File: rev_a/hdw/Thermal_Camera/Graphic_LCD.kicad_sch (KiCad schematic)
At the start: 0 parts

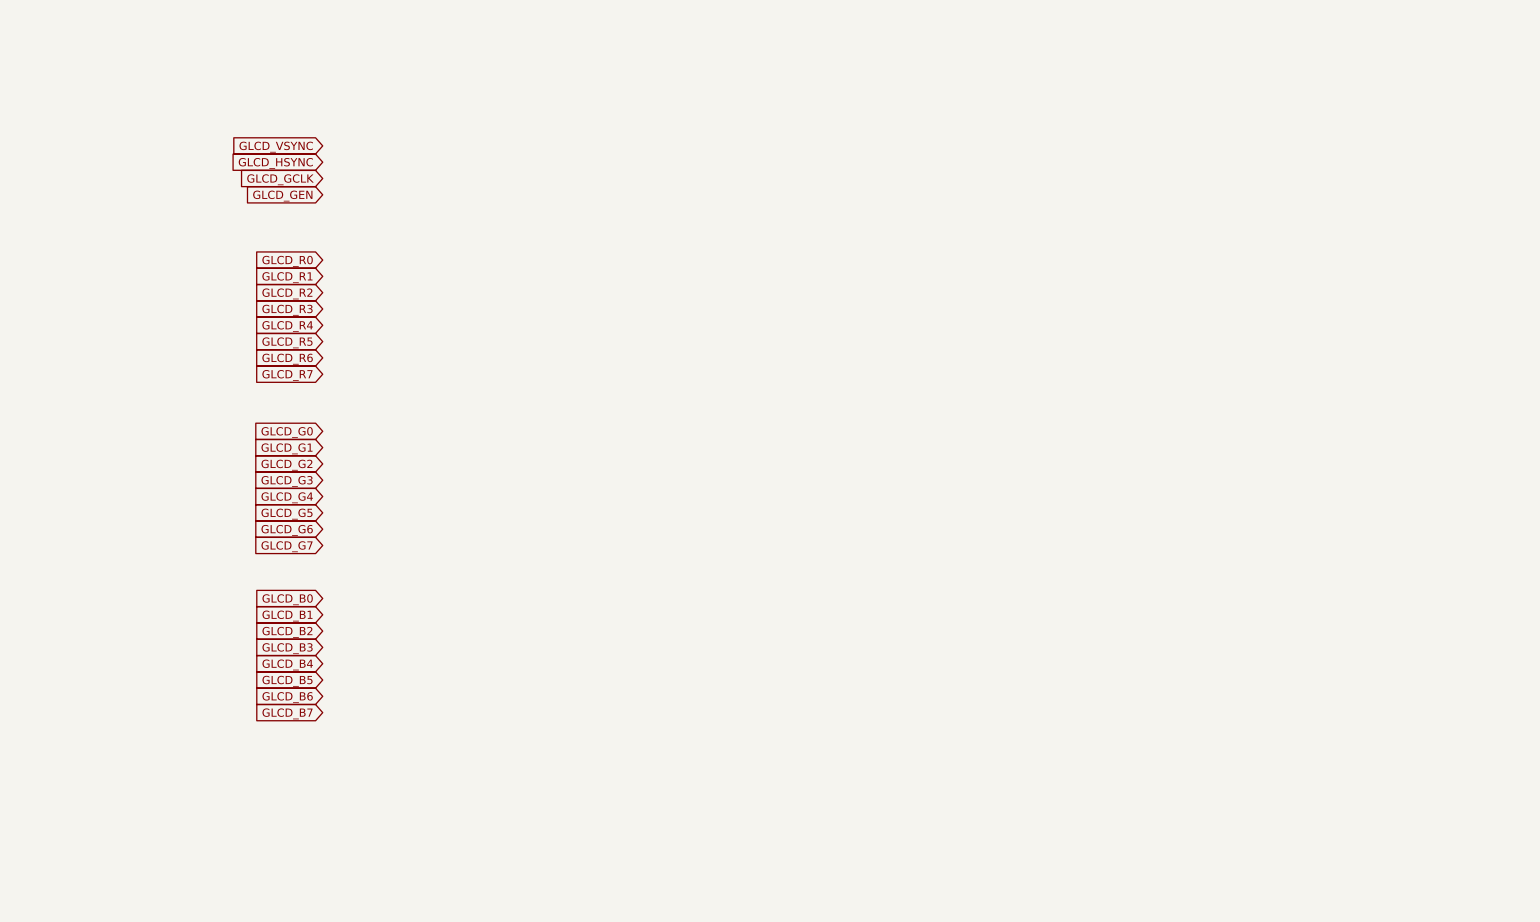
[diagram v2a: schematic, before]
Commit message: added some LCD components
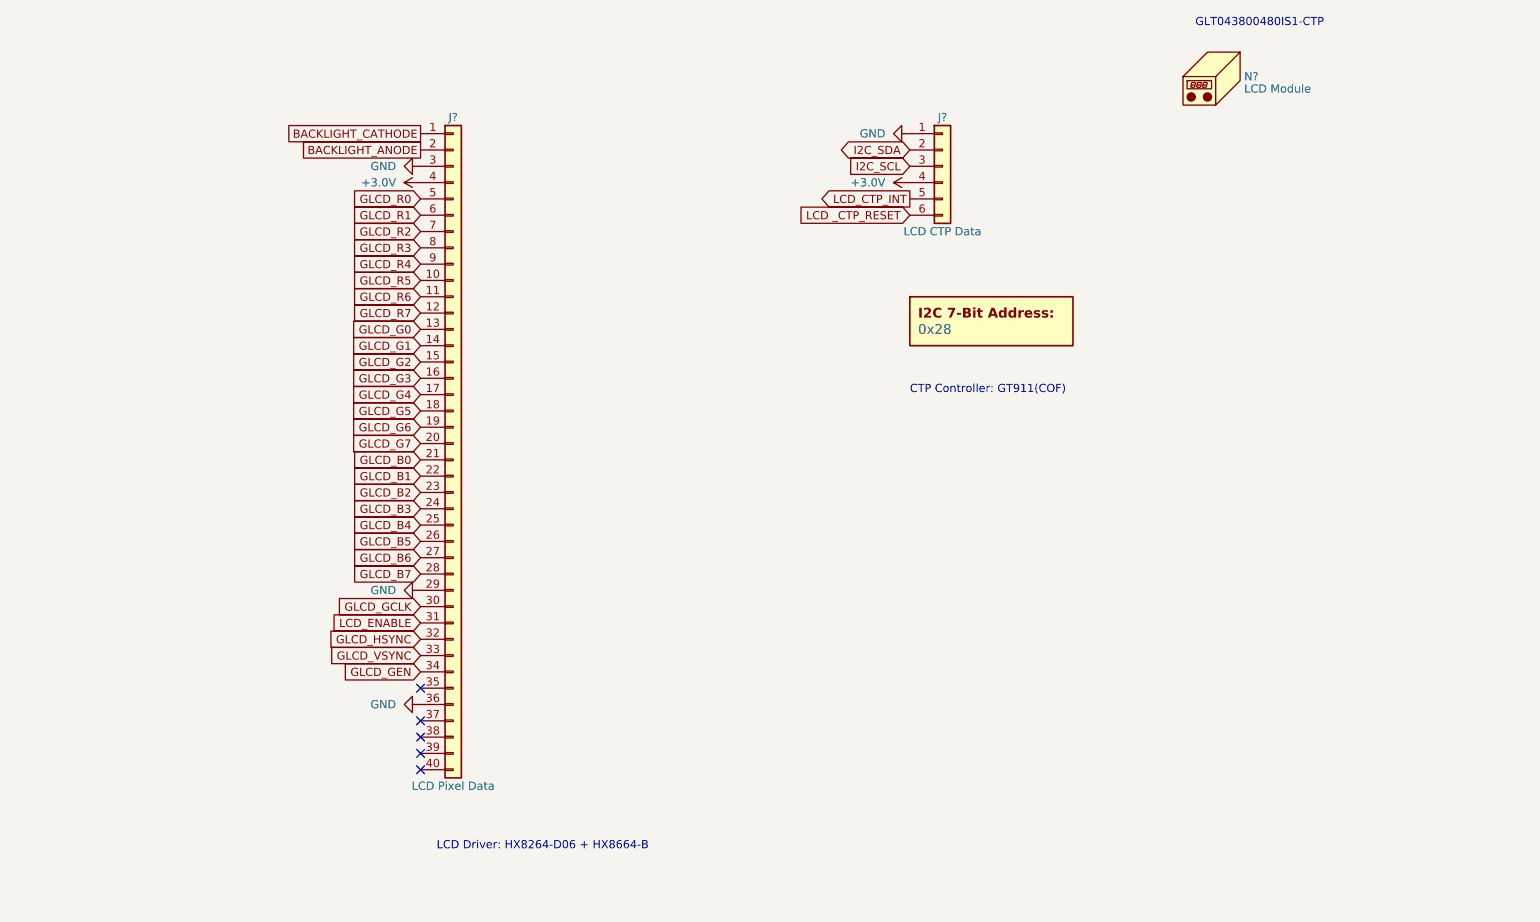
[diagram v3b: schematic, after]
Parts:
- added DOC?: 0x28, symbol Custom_Library:I2C_Address
- added J?: LCD Pixel Data, symbol Connector_Generic:Conn_01x40
- added J?: LCD CTP Data, symbol Connector_Generic:Conn_01x06
- added N?: LCD Module, symbol Mechanical:Housing
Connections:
- net GLCD_B0: now also J?.21 (Pin_21)
- net GLCD_B1: now also J?.22 (Pin_22)
- net GLCD_B2: now also J?.23 (Pin_23)
- net GLCD_B3: now also J?.24 (Pin_24)
- net GLCD_B4: now also J?.25 (Pin_25)
- net GLCD_B5: now also J?.26 (Pin_26)
- net GLCD_B6: now also J?.27 (Pin_27)
- net GLCD_B7: now also J?.28 (Pin_28)
- net GLCD_G0: now also J?.13 (Pin_13)
- net GLCD_G1: now also J?.14 (Pin_14)
- net GLCD_G2: now also J?.15 (Pin_15)
- net GLCD_G3: now also J?.16 (Pin_16)
- net GLCD_G4: now also J?.17 (Pin_17)
- net GLCD_G5: now also J?.18 (Pin_18)
- net GLCD_G6: now also J?.19 (Pin_19)
- net GLCD_G7: now also J?.20 (Pin_20)
- net GLCD_GCLK: now also J?.30 (Pin_30)
- net GLCD_GEN: now also J?.34 (Pin_34)
- net GLCD_HSYNC: now also J?.32 (Pin_32)
- net GLCD_R0: now also J?.5 (Pin_5)
- net GLCD_R1: now also J?.6 (Pin_6)
- net GLCD_R2: now also J?.7 (Pin_7)
- net GLCD_R3: now also J?.8 (Pin_8)
- net GLCD_R4: now also J?.9 (Pin_9)
- net GLCD_R5: now also J?.10 (Pin_10)
- net GLCD_R6: now also J?.11 (Pin_11)
- net GLCD_R7: now also J?.12 (Pin_12)
- net GLCD_VSYNC: now also J?.33 (Pin_33)
- new net +3.0V: J?.4 (Pin_4), J?.4 (Pin_4)
- new net BACKLIGHT_ANODE: J?.2 (Pin_2)
- new net BACKLIGHT_CATHODE: J?.1 (Pin_1)
- new net GND: J?.1 (Pin_1), J?.29 (Pin_29), J?.3 (Pin_3), J?.36 (Pin_36)
- new net I2C_SCL: J?.3 (Pin_3)
- new net I2C_SDA: J?.2 (Pin_2)
- new net LCD _CTP_RESET: J?.6 (Pin_6)
- new net LCD_CTP_INT: J?.5 (Pin_5)
- new net LCD_ENABLE: J?.31 (Pin_31)
- no-connect marks 0 -> 5
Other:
- note added: "CTP Controller: GT911(COF)"
- note added: "GLT043800480IS1-CTP"
- note added: "LCD Driver: HX8264-D06 + HX8664-B"

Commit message: added pull resistors for LCD signals
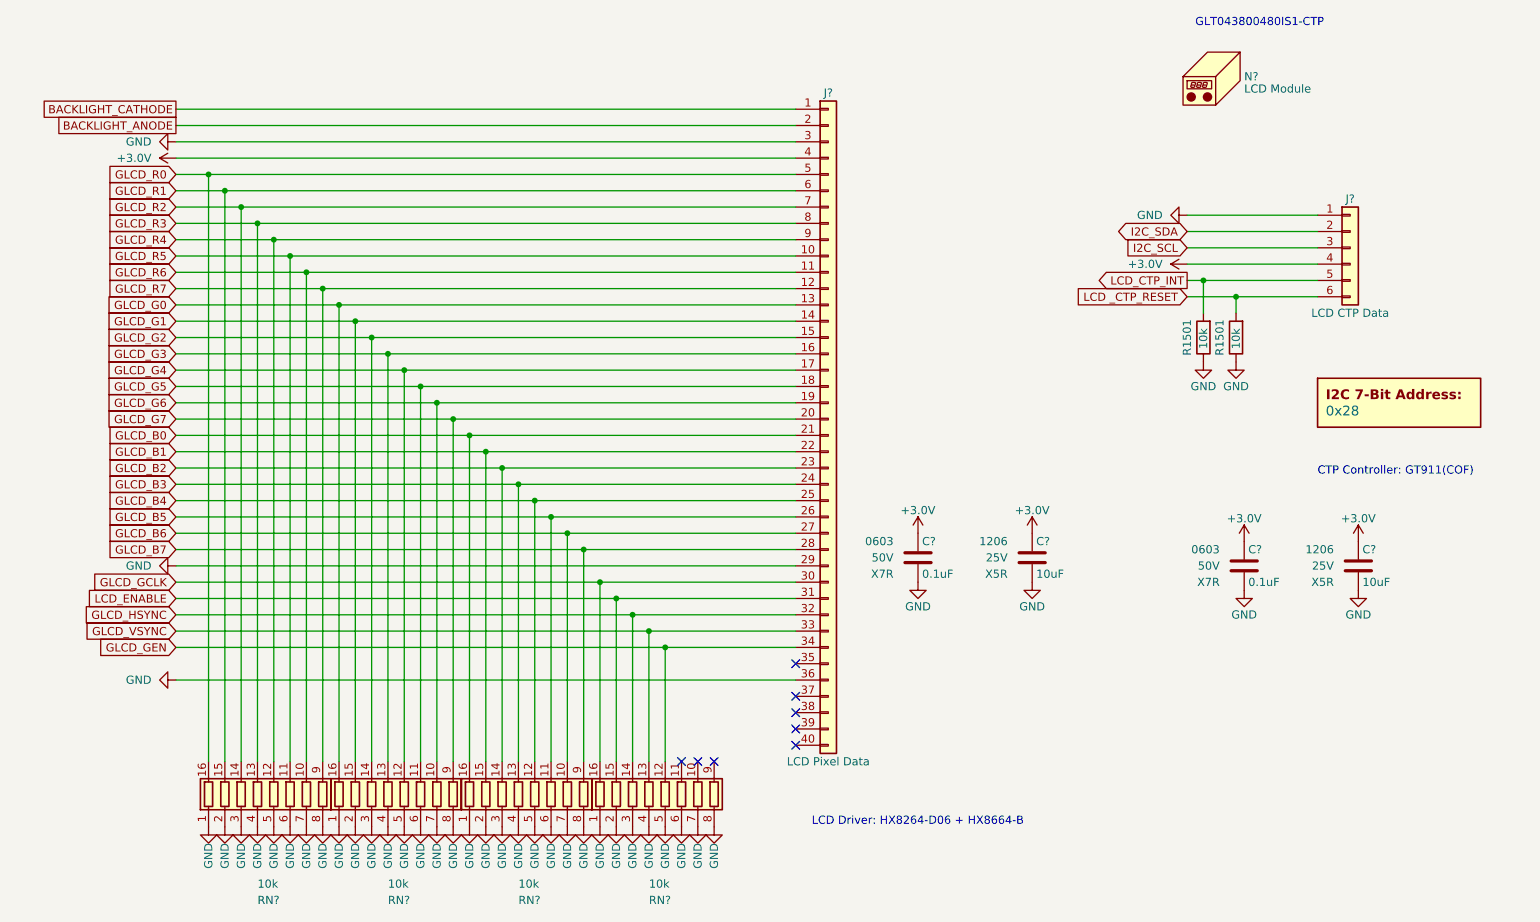
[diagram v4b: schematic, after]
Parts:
- added C? (x2): 0.1uF, Capacitors_SMD:C_0603, symbol Custom_Library:C_Custom
- added C? (x2): 10uF, Capacitors_SMD:C_1206, symbol Custom_Library:C_Custom
- added R1501 (x2): 10k, Resistors_SMD:R_0603, symbol Custom_Library:R_Custom
- added RN? (x4): 10k, Resistors_SMD:R_Array_Convex_8x0602, symbol Device:R_Pack08
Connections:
- net +3.0V: now also C?.1, C?.1, C?.1, C?.1
- net GLCD_B0: now also RN?.16 (R1.2)
- net GLCD_B1: now also RN?.15 (R2.2)
- net GLCD_B2: now also RN?.14 (R3.2)
- net GLCD_B3: now also RN?.13 (R4.2)
- net GLCD_B4: now also RN?.12 (R5.2)
- net GLCD_B5: now also RN?.11 (R6.2)
- net GLCD_B6: now also RN?.10 (R7.2)
- net GLCD_B7: now also RN?.9 (R8.2)
- net GLCD_G0: now also RN?.16 (R1.2)
- net GLCD_G1: now also RN?.15 (R2.2)
- net GLCD_G2: now also RN?.14 (R3.2)
- net GLCD_G3: now also RN?.13 (R4.2)
- net GLCD_G4: now also RN?.12 (R5.2)
- net GLCD_G5: now also RN?.11 (R6.2)
- net GLCD_G6: now also RN?.10 (R7.2)
- net GLCD_G7: now also RN?.9 (R8.2)
- net GLCD_GCLK: now also RN?.16 (R1.2)
- net GLCD_GEN: now also RN?.12 (R5.2)
- net GLCD_HSYNC: now also RN?.14 (R3.2)
- net GLCD_R0: now also RN?.16 (R1.2)
- net GLCD_R1: now also RN?.15 (R2.2)
- net GLCD_R2: now also RN?.14 (R3.2)
- net GLCD_R3: now also RN?.13 (R4.2)
- net GLCD_R4: now also RN?.12 (R5.2)
- net GLCD_R5: now also RN?.11 (R6.2)
- net GLCD_R6: now also RN?.10 (R7.2)
- net GLCD_R7: now also RN?.9 (R8.2)
- net GLCD_VSYNC: now also RN?.13 (R4.2)
- net GND: now also C?.2, C?.2, C?.2, C?.2, R1501.2, R1501.2, RN?.1 (R1.1), RN?.1 (R1.1), RN?.1 (R1.1), RN?.1 (R1.1), RN?.2 (R2.1), RN?.2 (R2.1), RN?.2 (R2.1), RN?.2 (R2.1), RN?.3 (R3.1), RN?.3 (R3.1), RN?.3 (R3.1), RN?.3 (R3.1), RN?.4 (R4.1), RN?.4 (R4.1), RN?.4 (R4.1), RN?.4 (R4.1), RN?.5 (R5.1), RN?.5 (R5.1), RN?.5 (R5.1), RN?.5 (R5.1), RN?.6 (R6.1), RN?.6 (R6.1), RN?.6 (R6.1), RN?.6 (R6.1), RN?.7 (R7.1), RN?.7 (R7.1), RN?.7 (R7.1), RN?.7 (R7.1), RN?.8 (R8.1), RN?.8 (R8.1), RN?.8 (R8.1), RN?.8 (R8.1)
- net LCD _CTP_RESET: now also R1501.1
- net LCD_CTP_INT: now also R1501.1
- net LCD_ENABLE: now also RN?.15 (R2.2)
- no-connect marks 5 -> 8
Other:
- moved on the sheet: J?

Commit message: lots of schematic progress
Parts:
- C? (x2): footprint Capacitors_SMD:C_0603 -> (none); Digi-Key PN 1276-1935-1-ND -> (none); display_footprint 0603 -> (none)
- R? (x2): renamed from R1501; footprint Resistors_SMD:R_0603 -> (none); Digi-Key PN 541-10.0KHCT-ND -> (none); Wattage 1/10W -> (none); display_footprint 0603 -> (none)
- gave numbers to parts that had none: 5

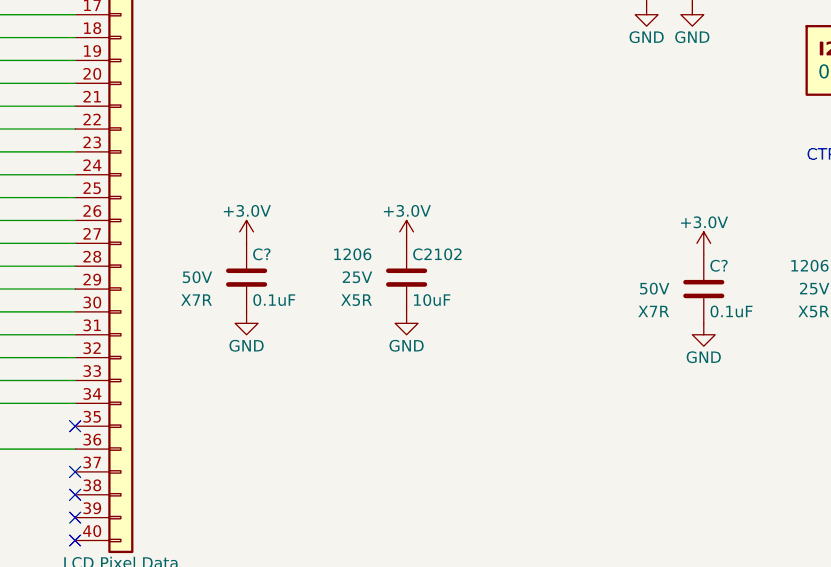
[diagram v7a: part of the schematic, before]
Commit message: assigned a ton of footprints
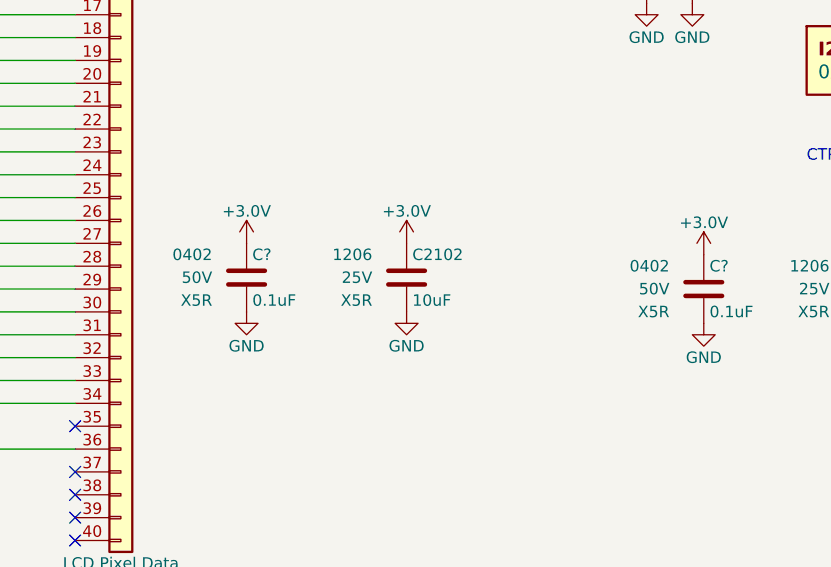
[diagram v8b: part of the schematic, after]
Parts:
- C? (x2): footprint (none) -> Capacitors_SMD:C_0402; Dielectric X7R -> X5R; display_footprint (none) -> 0402
- R? (x2): footprint (none) -> Resistors_SMD:R_0402; Wattage (none) -> 1/16W; display_footprint (none) -> 0402
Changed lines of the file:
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@@
 			)
 		)
-		(property "Footprint" ""
+		(property "Footprint" "Resistors_SMD:R_0402"
 			(at 215.9 71.12 0)
 			(effects
@@
 			)
 		)
-		(property "display_footprint" ""
+		(property "display_footprint" "0402"
 			(at 218.44 69.342 0)
 			(effects
@@
 			)
 		)
-		(property "Wattage" ""
+		(property "Wattage" "1/16W"
 			(at 218.44 74.422 0)
 			(effects
@@
 			)
 		)
-		(property "Footprint" ""
+		(property "Footprint" "Capacitors_SMD:C_0402"
 			(at 218.1352 110.49 0)
 			(effects
@@
 			)
 		)
-		(property "display_footprint" ""
+		(property "display_footprint" "0402"
 			(at 213.36 104.14 0)
 			(effects
@@
 			)
 		)
-		(property "Dielectric" "X7R"
+		(property "Dielectric" "X5R"
 			(at 213.36 109.22 0)
 			(effects
@@
 			)
 		)
-		(property "Footprint" ""
+		(property "Footprint" "Capacitors_SMD:C_0402"
 			(at 167.3352 109.22 0)
 			(effects
@@
 			)
 		)
-		(property "display_footprint" ""
+		(property "display_footprint" "0402"
 			(at 162.56 102.87 0)
 			(effects
@@
 			)
 		)
-		(property "Dielectric" "X7R"
+		(property "Dielectric" "X5R"
 			(at 162.56 107.95 0)
 			(effects
@@
 			)
 		)
-		(property "Footprint" ""
+		(property "Footprint" "Resistors_SMD:R_0402"
 			(at 210.82 71.12 0)
 			(effects
@@
 			)
 		)
-		(property "display_footprint" ""
+		(property "display_footprint" "0402"
 			(at 213.36 69.342 0)
 			(effects
@@
 			)
 		)
-		(property "Wattage" ""
+		(property "Wattage" "1/16W"
 			(at 213.36 74.422 0)
 			(effects
